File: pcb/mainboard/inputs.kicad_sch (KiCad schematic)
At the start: 110 parts, among them U10 MAX40026, U11 MAX40026, U12 MAX40026, U13 MAX40026, U14 MAX40026, U15 MAX40026, U16 MAX40026, U17 MAX40026, U18 MAX40026, U19 MAX40026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

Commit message: Initial FPGA routing
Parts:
- removed D11, D12, D13, D14: SZESD7471N2T5G, azonenberg_pcb:SOD882, symbol device:D_TVS
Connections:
- net CLK_200_N: now also U8.Y7 (IO_L12N_T1_MRCC_33); no longer U8.T3 (IO_L12N_T1_MRCC_34)
- net CLK_200_P: now also U8.Y8 (IO_L12P_T1_MRCC_33); no longer U8.R3 (IO_L12P_T1_MRCC_34)
- net TRIGIN_0_N: now also U8.AB5 (IO_L1N_T0_33); no longer U8.M3 (IO_L1N_T0_34)
- net TRIGIN_0_P: now also U8.AA5 (IO_L1P_T0_33); no longer U8.L3 (IO_L1P_T0_34)
- net TRIGIN_10_N: now also U8.W10 (IO_L15N_T2_DQS_33); no longer U8.V2 (IO_L15N_T2_DQS_34)
- net TRIGIN_10_P: now also U8.V10 (IO_L15P_T2_DQS_33); no longer U8.U2 (IO_L15P_T2_DQS_34)
- net TRIGIN_11_N: now also U8.T10 (IO_L16N_T2_33); no longer U8.U5 (IO_L16N_T2_34)
- net TRIGIN_11_P: now also U8.T11 (IO_L16P_T2_33); no longer U8.T5 (IO_L16P_T2_34)
- net TRIGIN_1_N: now also U8.AB7 (IO_L2N_T0_33); no longer U8.L1 (IO_L2N_T0_34)
- net TRIGIN_1_P: now also U8.AB8 (IO_L2P_T0_33); no longer U8.K1 (IO_L2P_T0_34)
- net TRIGIN_2_N: now also U8.AB6 (IO_L3N_T0_DQS_33); no longer U8.M1 (IO_L3N_T0_DQS_34)
- net TRIGIN_2_P: now also U8.AA6 (IO_L3P_T0_DQS_33); no longer U8.M2 (IO_L3P_T0_DQS_34)
- net TRIGIN_3_N: now also U8.AB10 (IO_L4N_T0_33); no longer U8.K2 (IO_L4N_T0_34)
- net TRIGIN_3_P: now also U8.AA10 (IO_L4P_T0_33); no longer U8.K3 (IO_L4P_T0_34)
- net TRIGIN_4_N: now also U8.AA8 (IO_L5N_T0_33); no longer U8.N2 (IO_L5N_T0_34)
- net TRIGIN_4_P: now also U8.AA9 (IO_L5P_T0_33); no longer U8.N3 (IO_L5P_T0_34)
- net TRIGIN_5_N: now also U8.Y11 (IO_L6N_T0_VREF_33); no longer U8.L4 (IO_L6N_T0_VREF_34)
- net TRIGIN_5_P: now also U8.W11 (IO_L6P_T0_33); no longer U8.L5 (IO_L6P_T0_34)
- net TRIGIN_6_N: now also U8.Y6 (IO_L7N_T1_33); no longer U8.R2 (IO_L7N_T1_34)
- net TRIGIN_6_P: now also U8.W6 (IO_L7P_T1_33); no longer U8.P2 (IO_L7P_T1_34)
- net TRIGIN_7_N: now also U8.R6 (IO_L8N_T1_33); no longer U8.R1 (IO_L8N_T1_34)
- net TRIGIN_7_P: now also U8.R7 (IO_L8P_T1_33); no longer U8.P1 (IO_L8P_T1_34)
- net TRIGIN_8_N: now also U8.V8 (IO_L9N_T1_DQS_33); no longer U8.N4 (IO_L9N_T1_DQS_34)
- net TRIGIN_8_P: now also U8.U8 (IO_L9P_T1_DQS_33); no longer U8.M5 (IO_L9P_T1_DQS_34)
- net TRIGIN_9_N: now also U8.U6 (IO_L10N_T1_33); no longer U8.U1 (IO_L10N_T1_34)
- net TRIGIN_9_P: now also U8.U7 (IO_L10P_T1_33); no longer U8.T1 (IO_L10P_T1_34)
- net VREF_IN0: now also U21.11 (OUT7); no longer U21.2 (OUT0)
- net VREF_IN1: now also U21.10 (OUT6); no longer U21.3 (OUT1)
- net VREF_IN2: now also U21.3 (OUT1); no longer U21.4 (OUT2)
- net VREF_IN3: now also U21.2 (OUT0); no longer U21.5 (OUT3)
- net VREF_IN4: now also U21.9 (OUT5); no longer U21.8 (OUT4)
- net VREF_IN5: now also U21.8 (OUT4); no longer U21.9 (OUT5)
- net VREF_IN6: now also U21.5 (OUT3); no longer U21.10 (OUT6)
- net VREF_IN7: now also U21.4 (OUT2); no longer U21.11 (OUT7)
- net at R102.2: now also U8.T14 (IO_25_VRP_33); no longer U8.V5 (IO_25_VRP_34)
- net at R101.2: now also U8.T6 (IO_0_VRN_33); no longer U8.K4 (IO_0_VRN_34)

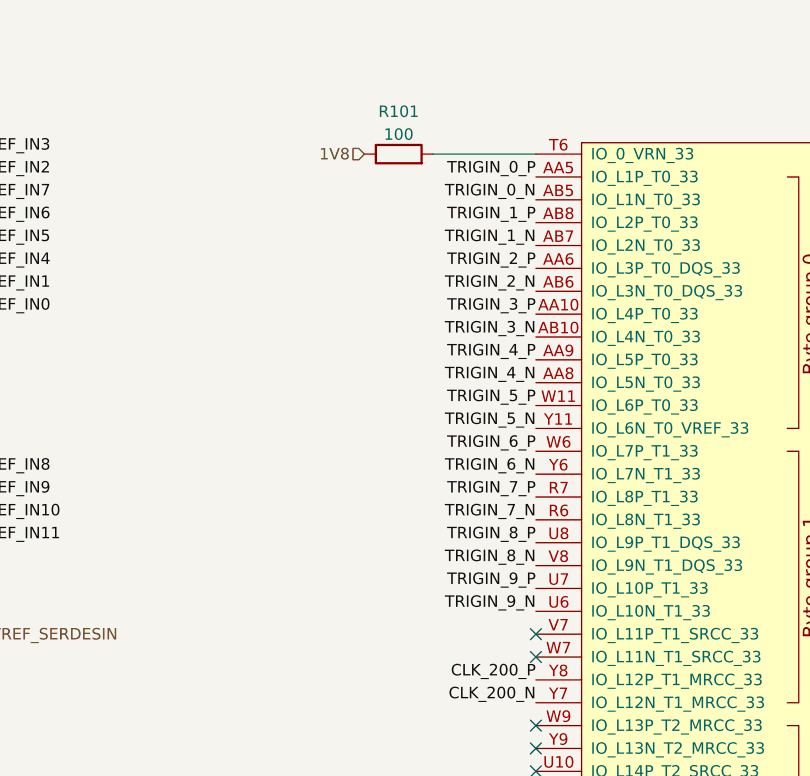
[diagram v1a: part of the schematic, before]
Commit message: Hooked up most input pins
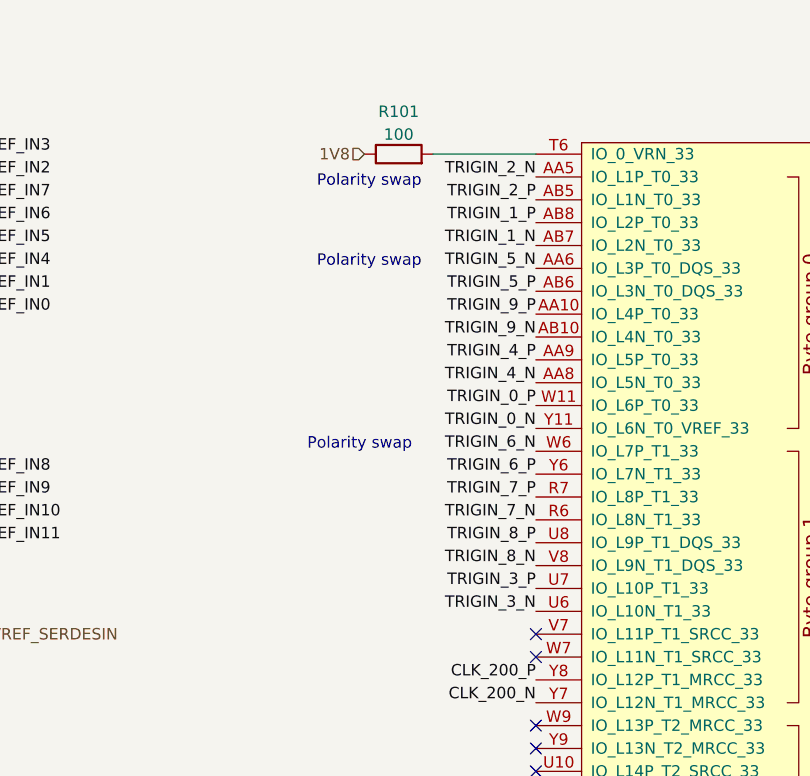
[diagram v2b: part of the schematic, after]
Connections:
- net TRIGIN_0_N: now also U8.Y11 (IO_L6N_T0_VREF_33); no longer U8.AB5 (IO_L1N_T0_33)
- net TRIGIN_0_P: now also U8.W11 (IO_L6P_T0_33); no longer U8.AA5 (IO_L1P_T0_33)
- net TRIGIN_2_N: now also U8.AA5 (IO_L1P_T0_33); no longer U8.AB6 (IO_L3N_T0_DQS_33)
- net TRIGIN_2_P: now also U8.AB5 (IO_L1N_T0_33); no longer U8.AA6 (IO_L3P_T0_DQS_33)
- net TRIGIN_3_N: now also U8.U6 (IO_L10N_T1_33); no longer U8.AB10 (IO_L4N_T0_33)
- net TRIGIN_3_P: now also U8.U7 (IO_L10P_T1_33); no longer U8.AA10 (IO_L4P_T0_33)
- net TRIGIN_5_N: now also U8.AA6 (IO_L3P_T0_DQS_33); no longer U8.Y11 (IO_L6N_T0_VREF_33)
- net TRIGIN_5_P: now also U8.AB6 (IO_L3N_T0_DQS_33); no longer U8.W11 (IO_L6P_T0_33)
- net TRIGIN_6_N: now also U8.W6 (IO_L7P_T1_33); no longer U8.Y6 (IO_L7N_T1_33)
- net TRIGIN_6_P: now also U8.Y6 (IO_L7N_T1_33); no longer U8.W6 (IO_L7P_T1_33)
- net TRIGIN_9_N: now also U8.AB10 (IO_L4N_T0_33); no longer U8.U6 (IO_L10N_T1_33)
- net TRIGIN_9_P: now also U8.AA10 (IO_L4P_T0_33); no longer U8.U7 (IO_L10P_T1_33)
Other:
- note added: "Polarity swap"
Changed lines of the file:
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@@
     (effects (font (size 1.27 1.27)) (justify left bottom))
+  )
+  (text "Polarity swap" (at 259.08 40.64 180)
+    (effects (font (size 1.27 1.27)) (justify right bottom))
   )
   (text "6 dB attenuator\n1206 for 150 ohm" (at 53.34 237.49 0)
@@
     (effects (font (size 1.27 1.27)) (justify left bottom))
   )
+  (text "Polarity swap" (at 259.08 31.75 180)
+    (effects (font (size 1.27 1.27)) (justify right bottom))
+  )
   (text "6 dB attenuator\n1206 for 150 ohm" (at 53.34 332.74 0)
     (effects (font (size 1.27 1.27)) (justify left bottom))
   )
+  (text "Polarity swap" (at 246.38 60.96 0)
+    (effects (font (size 1.27 1.27)) (justify left bottom))
+  )
   (text "6 dB attenuator\n1206 for 150 ohm" (at 53.34 142.24 0)
     (effects (font (size 1.27 1.27)) (justify left bottom))
@@
     (effects (font (size 1.27 1.27)) (justify right bottom))
   )
-  (label "TRIGIN_5_N" (at 271.78 58.42 180)
+  (label "TRIGIN_5_N" (at 271.78 40.64 180)
     (effects (font (size 1.27 1.27)) (justify right bottom))
   )
@@
     (effects (font (size 1.27 1.27)) (justify right bottom))
   )
-  (label "TRIGIN_5_P" (at 271.78 55.88 180)
+  (label "TRIGIN_5_P" (at 271.78 43.18 180)
     (effects (font (size 1.27 1.27)) (justify right bottom))
   )
@@
     (effects (font (size 1.27 1.27)) (justify right bottom))
   )
-  (label "TRIGIN_6_P" (at 271.78 60.96 180)
+  (label "TRIGIN_6_P" (at 271.78 63.5 180)
     (effects (font (size 1.27 1.27)) (justify right bottom))
   )
@@
     (effects (font (size 1.27 1.27)) (justify right bottom))
   )
-  (label "TRIGIN_2_P" (at 271.78 40.64 180)
+  (label "TRIGIN_2_P" (at 271.78 33.02 180)
     (effects (font (size 1.27 1.27)) (justify right bottom))
   )
@@
     (effects (font (size 1.27 1.27)) (justify right bottom))
   )
-  (label "TRIGIN_3_N" (at 271.78 48.26 180)
+  (label "TRIGIN_3_N" (at 271.78 78.74 180)
     (effects (font (size 1.27 1.27)) (justify right bottom))
   )
@@
     (effects (font (size 1.27 1.27)) (justify right bottom))
   )
-  (label "TRIGIN_0_N" (at 271.78 33.02 180)
+  (label "TRIGIN_0_N" (at 271.78 58.42 180)
     (effects (font (size 1.27 1.27)) (justify right bottom))
   )
@@
     (effects (font (size 1.27 1.27)) (justify left bottom))
   )
-  (label "TRIGIN_9_P" (at 271.78 76.2 180)
+  (label "TRIGIN_9_P" (at 271.78 45.72 180)
     (effects (font (size 1.27 1.27)) (justify right bottom))
   )
@@
     (effects (font (size 1.27 1.27)) (justify right bottom))
   )
-  (label "TRIGIN_9_N" (at 271.78 78.74 180)
+  (label "TRIGIN_9_N" (at 271.78 48.26 180)
     (effects (font (size 1.27 1.27)) (justify right bottom))
   )
@@
     (effects (font (size 1.27 1.27)) (justify left bottom))
   )
-  (label "TRIGIN_0_P" (at 271.78 30.48 180)
+  (label "TRIGIN_0_P" (at 271.78 55.88 180)
     (effects (font (size 1.27 1.27)) (justify right bottom))
   )
@@
     (effects (font (size 1.27 1.27)) (justify right bottom))
   )
-  (label "TRIGIN_3_P" (at 271.78 45.72 180)
-    (effects (font (size 1.27 1.27)) (justify right bottom))
-  )
-  (label "TRIGIN_2_N" (at 271.78 43.18 180)
+  (label "TRIGIN_3_P" (at 271.78 76.2 180)
+    (effects (font (size 1.27 1.27)) (justify right bottom))
+  )
+  (label "TRIGIN_2_N" (at 271.78 30.48 180)
     (effects (font (size 1.27 1.27)) (justify right bottom))
   )
@@
     (effects (font (size 1.27 1.27)) (justify right bottom))
   )
-  (label "TRIGIN_6_N" (at 271.78 63.5 180)
-    (effects (font (size 1.27 1.27)) (justify right bottom))
-  )
+  (label "TRIGIN_6_N" (at 271.78 60.96 180)
+    (effects (font (size 1.27 1.27)) (justify right bottom))
+  )

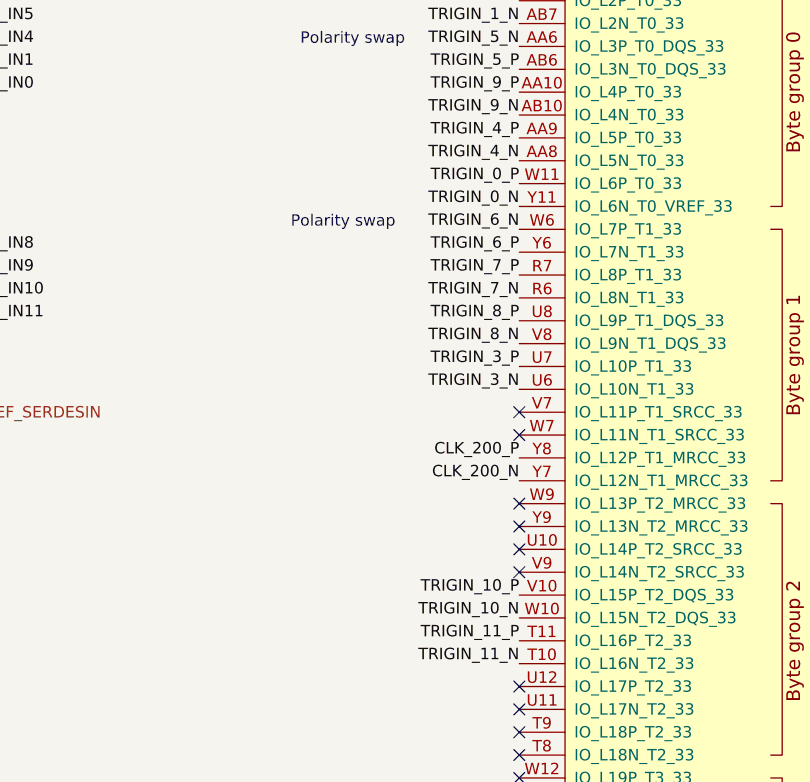
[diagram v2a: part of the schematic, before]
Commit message: Hooked up PMOD, initial placement of FPGA JTAG
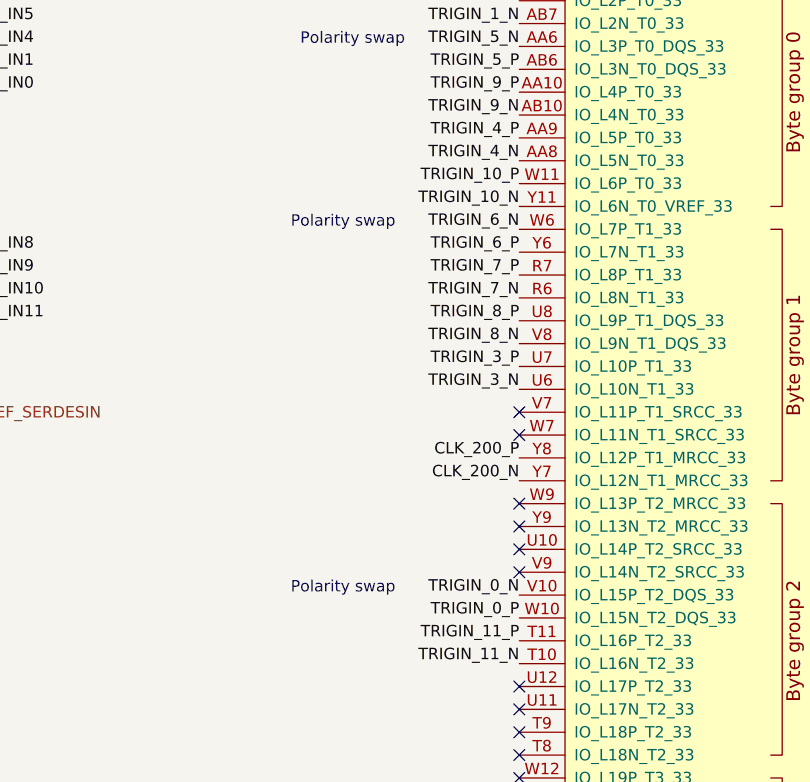
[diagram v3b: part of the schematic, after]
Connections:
- net TRIGIN_0_N: now also U8.V10 (IO_L15P_T2_DQS_33); no longer U8.Y11 (IO_L6N_T0_VREF_33)
- net TRIGIN_0_P: now also U8.W10 (IO_L15N_T2_DQS_33); no longer U8.W11 (IO_L6P_T0_33)
- net TRIGIN_10_N: now also U8.Y11 (IO_L6N_T0_VREF_33); no longer U8.W10 (IO_L15N_T2_DQS_33)
- net TRIGIN_10_P: now also U8.W11 (IO_L6P_T0_33); no longer U8.V10 (IO_L15P_T2_DQS_33)
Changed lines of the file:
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@@
+    (effects (font (size 1.27 1.27)) (justify left bottom))
+  )
+  (text "Polarity swap" (at 246.38 101.6 0)
     (effects (font (size 1.27 1.27)) (justify left bottom))
   )
@@
     (effects (font (size 1.27 1.27)) (justify right bottom))
   )
-  (label "TRIGIN_10_P" (at 271.78 101.6 180)
+  (label "TRIGIN_10_P" (at 271.78 55.88 180)
     (effects (font (size 1.27 1.27)) (justify right bottom))
   )
@@
     (effects (font (size 1.27 1.27)) (justify right bottom))
   )
-  (label "TRIGIN_0_N" (at 271.78 58.42 180)
+  (label "TRIGIN_0_N" (at 271.78 101.6 180)
     (effects (font (size 1.27 1.27)) (justify right bottom))
   )
@@
     (effects (font (size 1.27 1.27)) (justify left bottom))
   )
-  (label "TRIGIN_0_P" (at 271.78 55.88 180)
+  (label "TRIGIN_0_P" (at 271.78 104.14 180)
     (effects (font (size 1.27 1.27)) (justify right bottom))
   )
@@
     (effects (font (size 1.27 1.27)) (justify right bottom))
   )
-  (label "TRIGIN_10_N" (at 271.78 104.14 180)
-    (effects (font (size 1.27 1.27)) (justify right bottom))
-  )
+  (label "TRIGIN_10_N" (at 271.78 58.42 180)
+    (effects (font (size 1.27 1.27)) (justify right bottom))
+  )

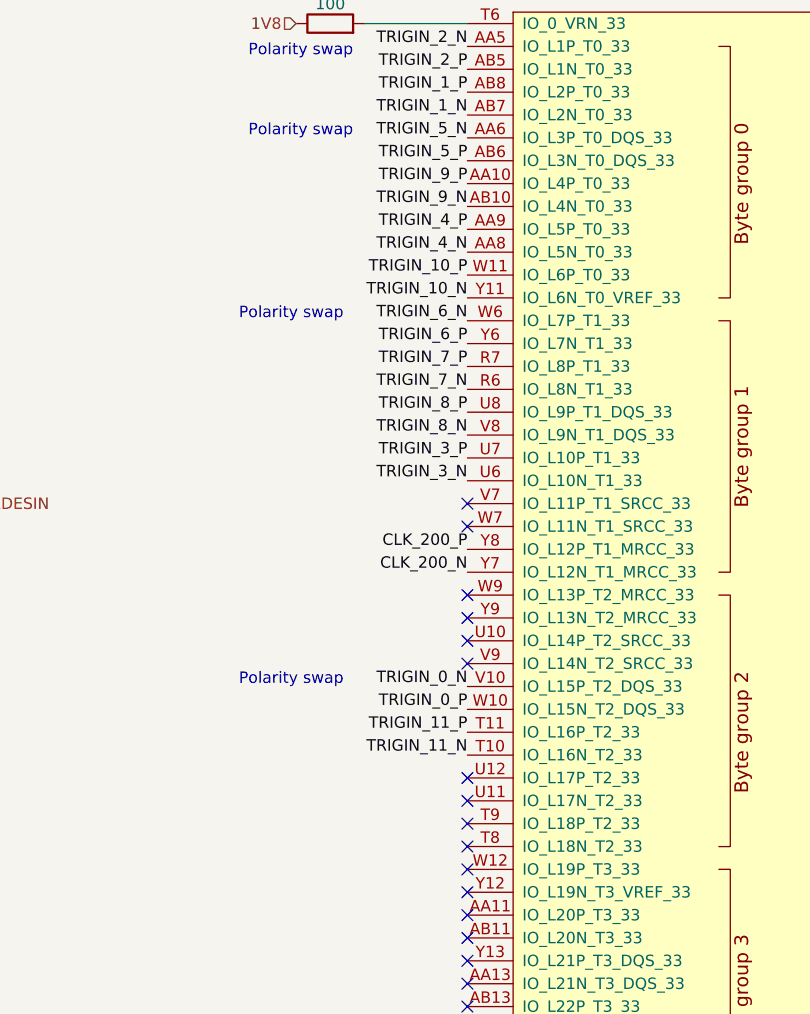
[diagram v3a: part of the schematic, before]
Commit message: Hooked up soft power/reset buttons
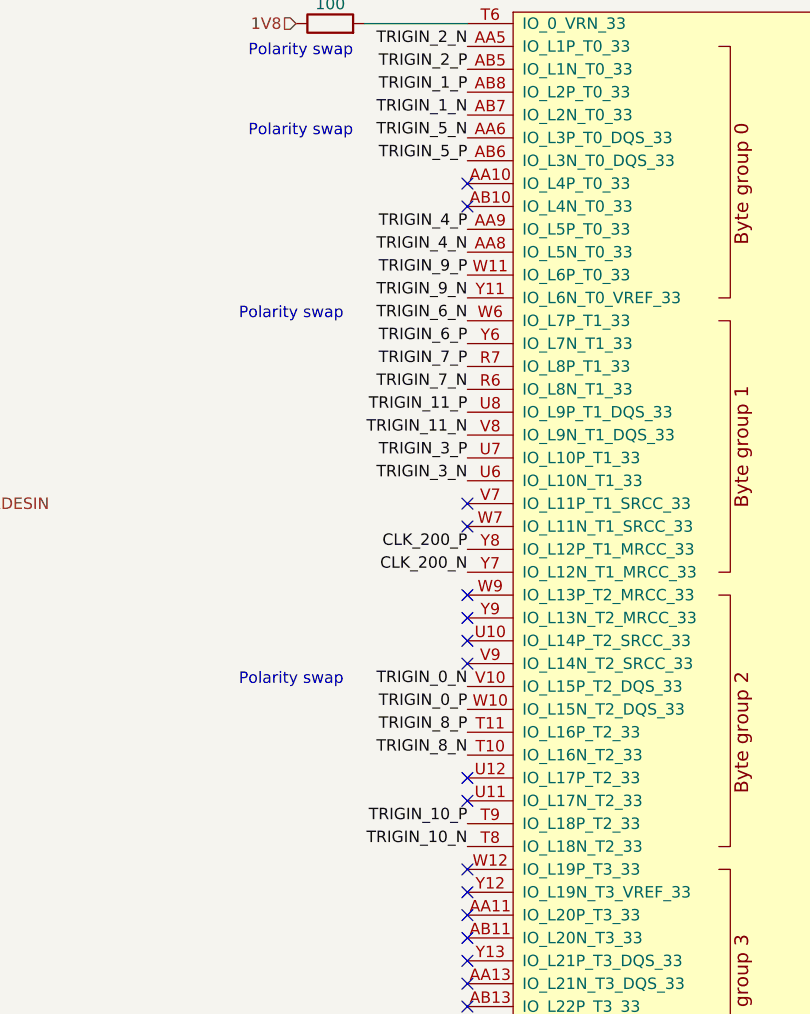
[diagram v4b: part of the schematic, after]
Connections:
- net TRIGIN_10_N: now also U8.T8 (IO_L18N_T2_33); no longer U8.Y11 (IO_L6N_T0_VREF_33)
- net TRIGIN_10_P: now also U8.T9 (IO_L18P_T2_33); no longer U8.W11 (IO_L6P_T0_33)
- net TRIGIN_11_N: now also U8.V8 (IO_L9N_T1_DQS_33); no longer U8.T10 (IO_L16N_T2_33)
- net TRIGIN_11_P: now also U8.U8 (IO_L9P_T1_DQS_33); no longer U8.T11 (IO_L16P_T2_33)
- net TRIGIN_8_N: now also U8.T10 (IO_L16N_T2_33); no longer U8.V8 (IO_L9N_T1_DQS_33)
- net TRIGIN_8_P: now also U8.T11 (IO_L16P_T2_33); no longer U8.U8 (IO_L9P_T1_DQS_33)
- net TRIGIN_9_N: now also U8.Y11 (IO_L6N_T0_VREF_33); no longer U8.AB10 (IO_L4N_T0_33)
- net TRIGIN_9_P: now also U8.W11 (IO_L6P_T0_33); no longer U8.AA10 (IO_L4P_T0_33)
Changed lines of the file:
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@@
   (junction (at 53.34 137.16) (diameter 0) (color 0 0 0 0)
   )
-  (no_connect (at 271.78 119.38))
   (no_connect (at 271.78 124.46))
   (no_connect (at 271.78 139.7))
@@
   (no_connect (at 271.78 111.76))
   (no_connect (at 271.78 144.78))
+  (no_connect (at 271.78 45.72))
   (no_connect (at 271.78 91.44))
+  (no_connect (at 271.78 48.26))
   (no_connect (at 271.78 132.08))
   (no_connect (at 271.78 142.24))
@@
   (no_connect (at 271.78 99.06))
   (no_connect (at 209.55 76.2))
-  (no_connect (at 271.78 116.84))
   (no_connect (at 271.78 137.16))
   (no_connect (at 209.55 78.74))
@@
     (effects (font (size 1.27 1.27)) (justify right bottom))
   )
-  (label "TRIGIN_10_P" (at 271.78 55.88 180)
+  (label "TRIGIN_10_P" (at 271.78 116.84 180)
     (effects (font (size 1.27 1.27)) (justify right bottom))
   )
@@
     (effects (font (size 1.27 1.27)) (justify right bottom))
   )
-  (label "TRIGIN_11_P" (at 271.78 106.68 180)
+  (label "TRIGIN_11_P" (at 271.78 71.12 180)
     (effects (font (size 1.27 1.27)) (justify right bottom))
   )
@@
     (effects (font (size 1.27 1.27)) (justify left bottom))
   )
-  (label "TRIGIN_9_P" (at 271.78 45.72 180)
+  (label "TRIGIN_9_P" (at 271.78 55.88 180)
     (effects (font (size 1.27 1.27)) (justify right bottom))
   )
@@
     (effects (font (size 1.27 1.27)) (justify right bottom))
   )
-  (label "TRIGIN_9_N" (at 271.78 48.26 180)
+  (label "TRIGIN_9_N" (at 271.78 58.42 180)
     (effects (font (size 1.27 1.27)) (justify right bottom))
   )
@@
     (effects (font (size 1.27 1.27)) (justify right bottom))
   )
-  (label "TRIGIN_8_N" (at 271.78 73.66 180)
+  (label "TRIGIN_8_N" (at 271.78 109.22 180)
     (effects (font (size 1.27 1.27)) (justify right bottom))
   )
@@
     (effects (font (size 1.27 1.27)) (justify right bottom))
   )
-  (label "TRIGIN_10_N" (at 271.78 58.42 180)
+  (label "TRIGIN_10_N" (at 271.78 119.38 180)
     (effects (font (size 1.27 1.27)) (justify right bottom))
   )
@@
     (effects (font (size 1.27 1.27)) (justify right bottom))
   )
-  (label "TRIGIN_8_P" (at 271.78 71.12 180)
+  (label "TRIGIN_8_P" (at 271.78 106.68 180)
     (effects (font (size 1.27 1.27)) (justify right bottom))
   )
@@
     (effects (font (size 1.27 1.27)) (justify left bottom))
   )
-  (label "TRIGIN_11_N" (at 271.78 109.22 180)
-    (effects (font (size 1.27 1.27)) (justify right bottom))
-  )
+  (label "TRIGIN_11_N" (at 271.78 73.66 180)
+    (effects (font (size 1.27 1.27)) (justify right bottom))
+  )
